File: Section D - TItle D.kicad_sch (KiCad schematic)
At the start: 0 parts

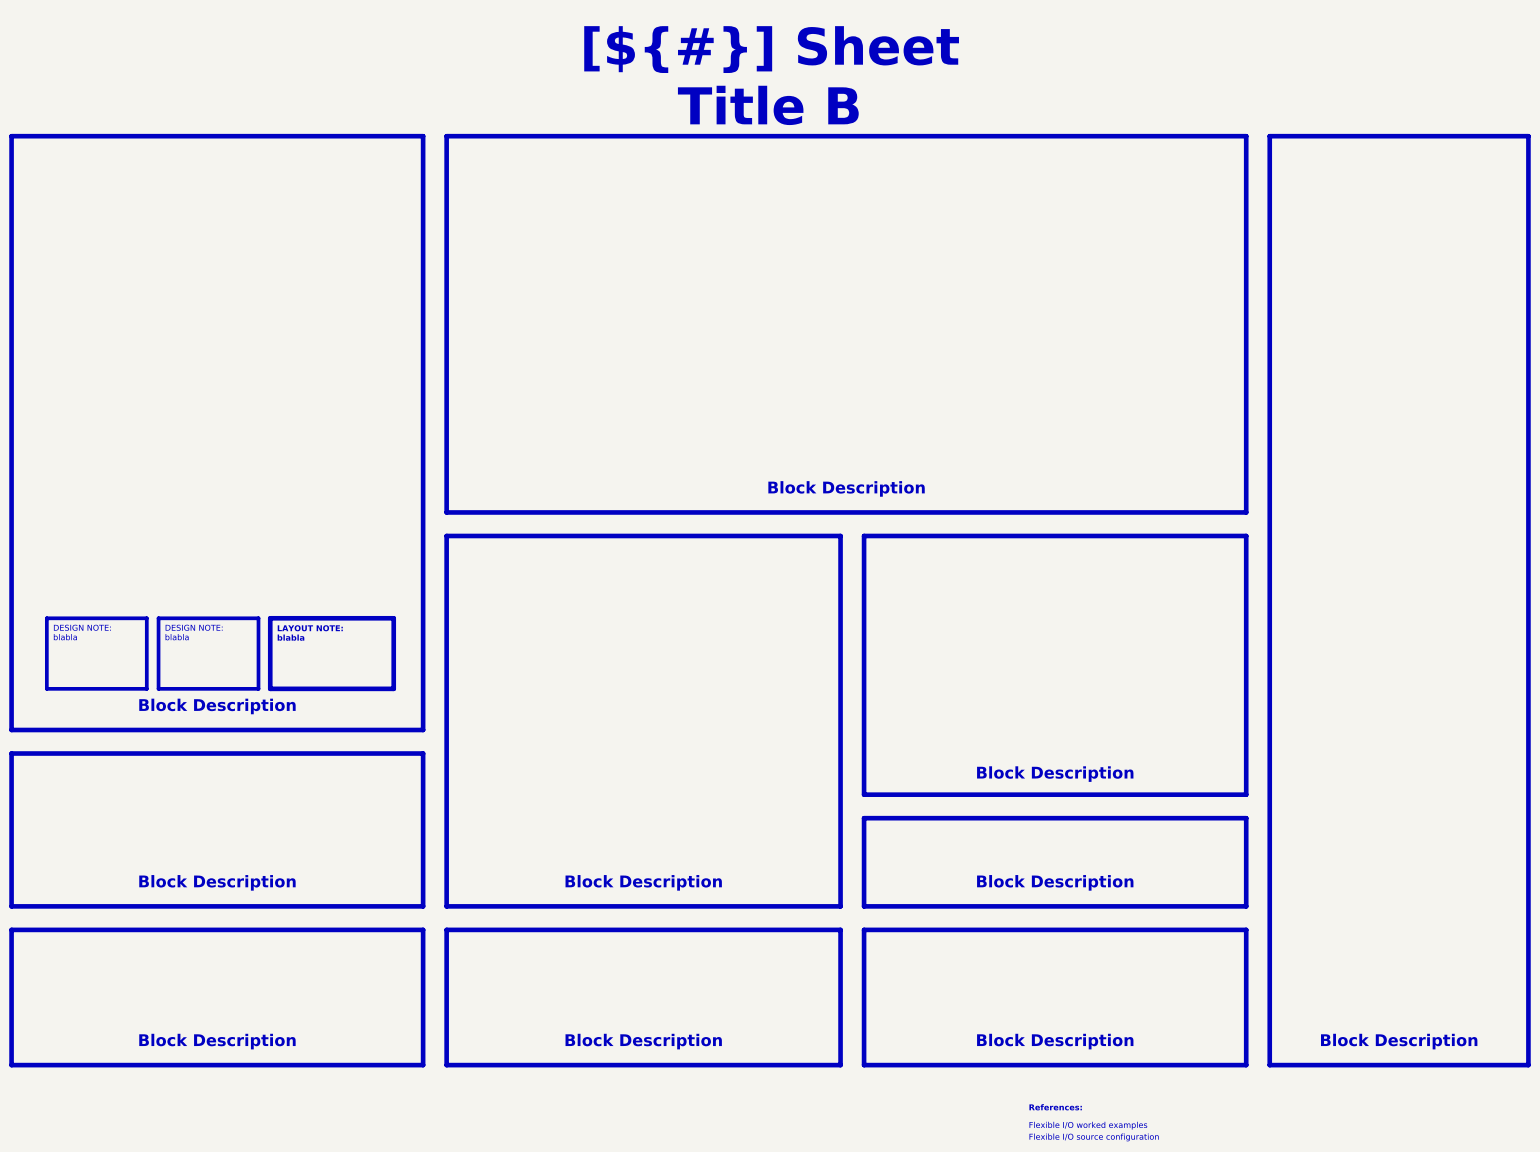
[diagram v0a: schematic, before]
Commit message: [FINISH LT3042 and ad TPS6108]
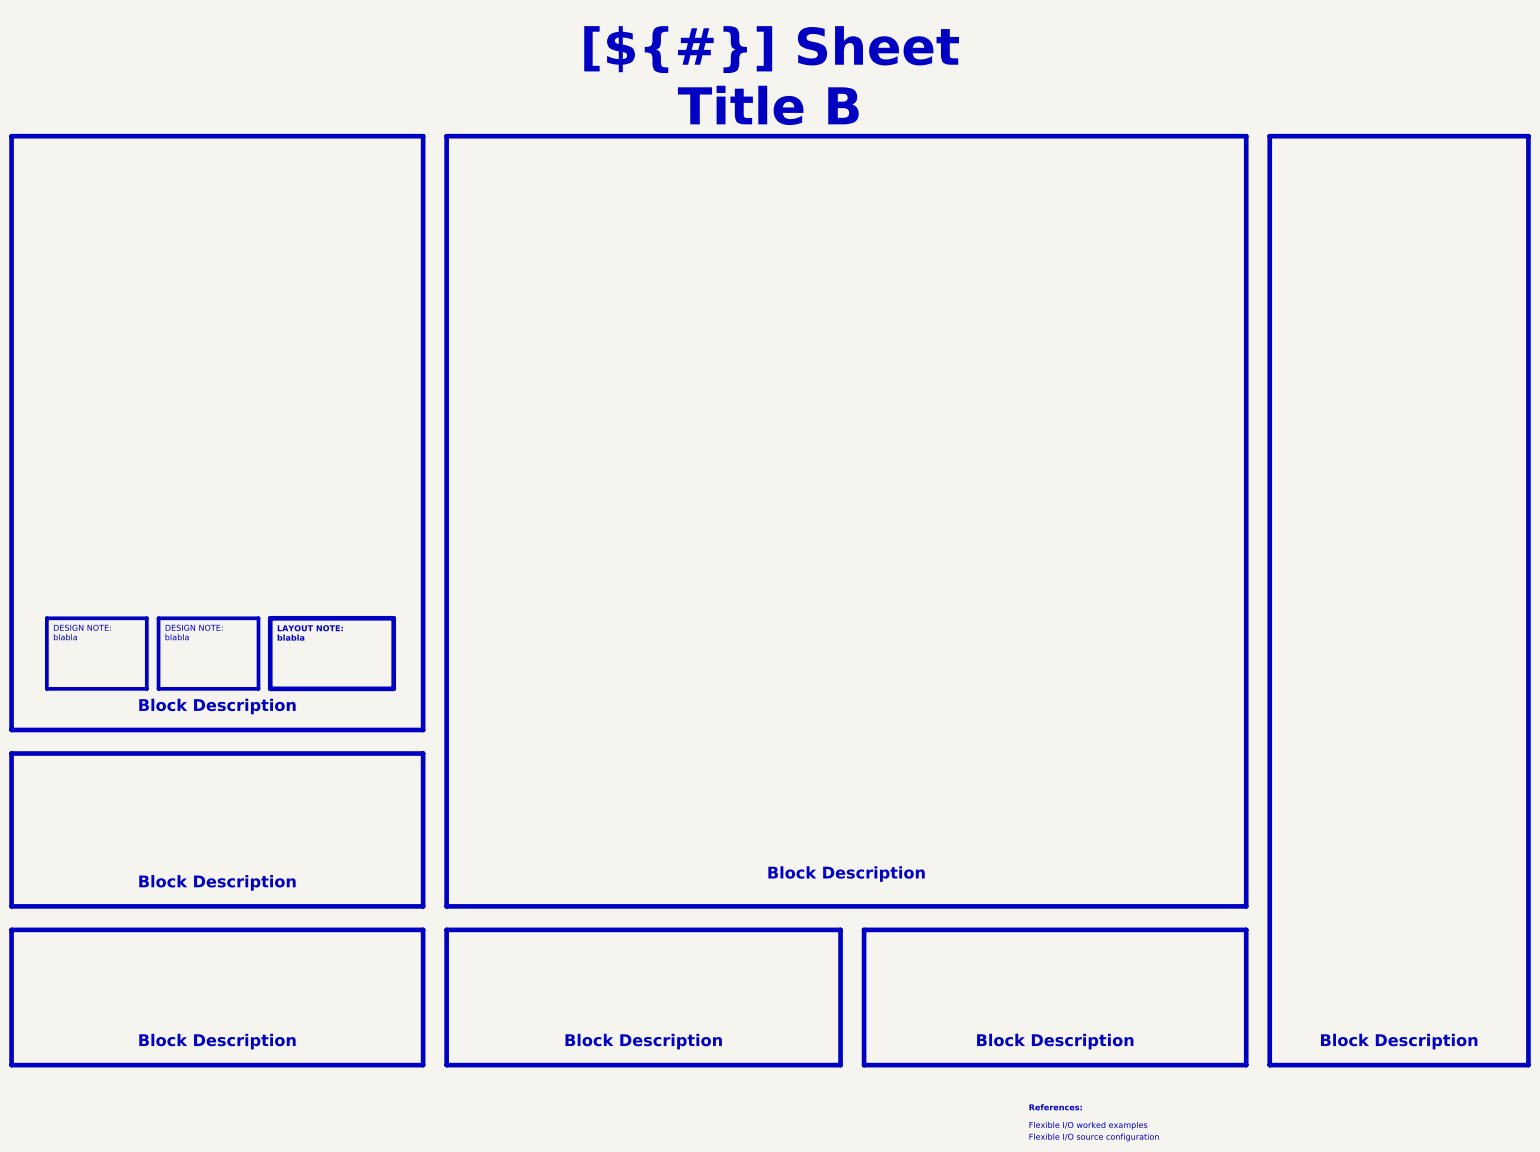
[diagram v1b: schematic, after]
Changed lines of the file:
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@@
-	)
-	(rectangle
-		(start 139.7 125.73)
-		(end 224.79 205.74)
-		(stroke
-			(width 1)
-			(type default)
-			(color 200 200 200 1)
-		)
-		(fill
-			(type none)
-		)
 	)
 	(rectangle
@@
 	)
 	(rectangle
-		(start 229.87 186.69)
-		(end 312.42 205.74)
-		(stroke
-			(width 1)
-			(type default)
-			(color 200 200 200 1)
-		)
-		(fill
-			(type none)
-		)
-	)
-	(rectangle
-		(start 229.87 125.73)
-		(end 312.42 181.61)
-		(stroke
-			(width 1)
-			(type default)
-			(color 200 200 200 1)
-		)
-		(fill
-			(type none)
-		)
-	)
-	(rectangle
 		(start 139.7 210.82)
 		(end 224.79 240.03)
@@
 	(rectangle
 		(start 139.7 39.37)
-		(end 312.42 120.65)
+		(end 312.42 205.74)
 		(stroke
 			(width 1)
@@
 	(text_box "Block Description"
 		(exclude_from_sim no)
-		(at 142.24 109.22 0)
+		(at 142.24 192.405 0)
 		(size 167.64 9.525)
-		(margins 1.9049 1.9049 1.9049 1.9049)
-		(stroke
-			(width -0.0001)
-			(type default)
-		)
-		(fill
-			(type none)
-		)
-		(effects
-			(font
-				(face "Times New Roman")
-				(size 2.54 2.54)
-				(thickness 0.508)
-				(bold yes)
-				(color 162 22 34 1)
-			)
-			(justify bottom)
-		)
-	)
-	(text_box "Block Description"
-		(exclude_from_sim no)
-		(at 231.775 170.815 0)
-		(size 78.74 9.525)
-		(margins 1.9049 1.9049 1.9049 1.9049)
-		(stroke
-			(width -0.0001)
-			(type default)
-		)
-		(fill
-			(type none)
-		)
-		(effects
-			(font
-				(face "Times New Roman")
-				(size 2.54 2.54)
-				(thickness 0.508)
-				(bold yes)
-				(color 162 22 34 1)
-			)
-			(justify bottom)
-		)
-	)
-	(text_box "Block Description"
-		(exclude_from_sim no)
-		(at 231.14 194.31 0)
-		(size 80.01 9.525)
 		(margins 1.9049 1.9049 1.9049 1.9049)
 		(stroke
@@
 		)
 	)
-	(text_box "Block Description"
-		(exclude_from_sim no)
-		(at 140.97 194.31 0)
-		(size 82.55 9.525)
-		(margins 1.9049 1.9049 1.9049 1.9049)
-		(stroke
-			(width -0.0001)
-			(type default)
-		)
-		(fill
-			(type none)
-		)
-		(effects
-			(font
-				(face "Times New Roman")
-				(size 2.54 2.54)
-				(thickness 0.508)
-				(bold yes)
-				(color 162 22 34 1)
-			)
-			(justify bottom)
-		)
-	)
